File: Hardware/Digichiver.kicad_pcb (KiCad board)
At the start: 4 copper layers, 95 x 88.1 mm, 121 parts, among them J1 DM3AT-SF-PEJM5, J2 USB4105-GF-A, J3 61300211121, J4 61300211121, J5 SJ1-3535NG, SW1 PTS_647_SN50_SMTR2_LFS, SW2 PTS_647_SN50_SMTR2_LFS, SW3 PTS_647_SN50_SMTR2_LFS, U1 RP2354B, U10 TLV9004IPWR, U11 PAM8302AAD, U2 SN74LVC245A, U3 SN74LVC245A, U4 SN74LVC8T245, U5 SN74LVC8T245, U6 SN74LVC8T245, U7 TLV61046A, U8 TPSM84338, U9 PCM1809, X2 ABM8-272-T3

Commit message: generate outputs
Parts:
- C34: footprint Capacitor_SMD:C_0603_1608Metric -> Capacitor_SMD:C_0402_1005Metric
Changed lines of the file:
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@@
 		)
 	)
-	(footprint "Capacitor_SMD:C_0603_1608Metric"
+	(footprint "Capacitor_SMD:C_0402_1005Metric"
 		(layer "B.Cu")
 		(at 114.3 65.302 90)
-		(descr "Capacitor SMD 0603 (1608 Metric), square (rectangular) end terminal, IPC-7351 nominal, (Body size source: IPC-SM-782 page 76, https://www.pcb-3d.com/wordpress/wp-content/uploads/ipc-sm-782a_amendment_1_and_2.pdf)")
+		(descr "Capacitor SMD 0402 (1005 Metric), square (rectangular) end terminal, IPC-7351 nominal, (Body size source: IPC-SM-782 page 76, https://www.pcb-3d.com/wordpress/wp-content/uploads/ipc-sm-782a_amendment_1_and_2.pdf)")
 		(tags "capacitor")
 		(property "Reference" "C34"
-			(at 0 1.43 270)
-			(unlocked yes)
+			(at 0 1.16 270)
 			(layer "B.SilkS")
 			(effects
@@
 		)
 		(property "Value" "4.7uF"
-			(at 0 -1.43 90)
+			(at 0 -1.16 270)
 			(layer "B.Fab")
 			(effects
@@
 			)
 		)
-		(property "Datasheet" "https://mm.digikey.com/Volume0/opasdata/d220001/medias/docus/43/CL10A475KA8NQNC_Spec.pdf"
-			(at 0 0 90)
+		(property "Datasheet" ""
+			(at 0 0 270)
 			(layer "B.Fab")
 			(hide yes)
@@
 			)
 		)
-		(property "Description" "Unpolarized capacitor"
-			(at 0 0 90)
+		(property "Description" ""
+			(at 0 0 270)
 			(layer "B.Fab")
 			(hide yes)
@@
 		)
 		(property "KiLib_Generator" "SMD_2terminal_chip_molded"
-			(at 0 0 90)
-			(layer "B.SilkS")
-			(hide yes)
-			(effects
-				(font
-					(size 1 1)
-					(thickness 0.15)
-				)
-				(justify mirror)
-			)
-		)
-		(property "Voltage" "25V"
-			(at 0 0 270)
-			(unlocked yes)
-			(layer "B.Fab")
-			(hide yes)
-			(effects
-				(font
-					(size 1 1)
-					(thickness 0.15)
-				)
-				(justify mirror)
-			)
-		)
-		(property "MPN" "CL10A475KA8NQNC"
-			(at 0 0 270)
-			(unlocked yes)
-			(layer "B.Fab")
-			(hide yes)
-			(effects
-				(font
-					(size 1 1)
-					(thickness 0.15)
-				)
-				(justify mirror)
-			)
-		)
-		(property "KLC_S4.2_DVDD" ""
 			(at 0 0 270)
-			(unlocked yes)
-			(layer "B.Fab")
-			(hide yes)
-			(effects
-				(font
-					(size 1 1)
-					(thickness 0.15)
-				)
-				(justify mirror)
-			)
-		)
-		(property "KLC_S4.2_VREG_LX" ""
-			(at 0 0 270)
-			(unlocked yes)
-			(layer "B.Fab")
+			(layer "B.SilkS")
 			(hide yes)
 			(effects
@@
 		(duplicate_pad_numbers_are_jumpers no)
 		(fp_line
-			(start -0.14058 -0.51)
-			(end 0.14058 -0.51)
+			(start -0.107836 -0.36)
+			(end 0.107836 -0.36)
 			(stroke
 				(width 0.12)
@@
 		)
 		(fp_line
-			(start -0.14058 0.51)
-			(end 0.14058 0.51)
+			(start -0.107836 0.36)
+			(end 0.107836 0.36)
 			(stroke
 				(width 0.12)
@@
 		)
 		(fp_rect
-			(start -1.48 0.73)
-			(end 1.48 -0.73)
+			(start -0.91 0.46)
+			(end 0.91 -0.46)
 			(stroke
 				(width 0.05)
@@
 		)
 		(fp_rect
-			(start -0.8 0.4)
-			(end 0.8 -0.4)
+			(start -0.5 0.25)
+			(end 0.5 -0.25)
 			(stroke
 				(width 0.1)
@@
 		(fp_text user "${REFERENCE}"
 			(at 0 0 270)
-			(unlocked yes)
 			(layer "B.Fab")
 			(effects
 				(font
-					(size 1 1)
-					(thickness 0.15)
+					(size 0.25 0.25)
+					(thickness 0.04)
 				)
 				(justify mirror)
@@
 		)
 		(pad "1" smd roundrect
-			(at -0.775 0 90)
-			(size 0.9 0.95)
+			(at -0.48 0 90)
+			(size 0.56 0.62)
 			(layers "B.Cu" "B.Mask" "B.Paste")
 			(roundrect_rratio 0.25)
@@
 		)
 		(pad "2" smd roundrect
-			(at 0.775 0 90)
-			(size 0.9 0.95)
+			(at 0.48 0 90)
+			(size 0.56 0.62)
 			(layers "B.Cu" "B.Mask" "B.Paste")
 			(roundrect_rratio 0.25)
@@
 		)
 		(embedded_fonts no)
-		(model "${KICAD10_3DMODEL_DIR}/Capacitor_SMD.3dshapes/C_0603_1608Metric.step"
+		(model "${KICAD10_3DMODEL_DIR}/Capacitor_SMD.3dshapes/C_0402_1005Metric.step"
 			(offset
 				(xyz 0 0 0)
@@
 	)
 	(segment
+		(start 115.062 65.278)
+		(end 114.756 65.278)
+		(width 0.2)
+		(layer "B.Cu")
+		(net "GND")
+	)
+	(segment
 		(start 114.272 60.734)
 		(end 114.3 60.706)
@@
 	)
 	(segment
+		(start 114.756 65.278)
+		(end 114.3 64.822)
+		(width 0.2)
+		(layer "B.Cu")
+		(net "GND")
+	)
+	(segment
 		(start 127.96 82.24)
 		(end 128.016 82.296)
@@
 	)
 	(segment
-		(start 114.3 64.527)
-		(end 114.311 64.527)
-		(width 0.2032)
-		(layer "B.Cu")
-		(net "GND")
-	)
-	(segment
 		(start 143.215 71.669)
 		(end 142.494 72.39)
@@
 	)
 	(segment
-		(start 114.311 64.527)
-		(end 115.062 65.278)
-		(width 0.2032)
-		(layer "B.Cu")
-		(net "GND")
-	)
-	(segment
 		(start 143.908 71.669)
 		(end 143.215 71.669)
@@
 	)
 	(segment
-		(start 114.3 66.077)
-		(end 115.303 66.077)
+		(start 115.316 66.064)
+		(end 114.582 66.064)
 		(width 0.2)
 		(layer "B.Cu")
@@
 	)
 	(segment
+		(start 114.582 66.064)
+		(end 114.3 65.782)
+		(width 0.2)
+		(layer "B.Cu")
+		(net "/Power/+9V_RAW")
+	)
+	(segment
 		(start 127.757598 70.61)
 		(end 127.757598 69.854402)
@@
 	)
 	(segment
-		(start 141.235 116.6545)
-		(end 141.235 126.394471)
-		(width 0.2)
-		(layer "F.Cu")
-		(net "/Digitalker/DIGI_ROM_ADDR0")
-	)
-	(segment
 		(start 141.235 130.804)
 		(end 137.668 134.371)
@@
 	)
 	(segment
-		(start 141.235 126.394471)
-		(end 141.132 126.497471)
-		(width 0.2)
-		(layer "F.Cu")
-		(net "/Digitalker/DIGI_ROM_ADDR0")
-	)
-	(segment
-		(start 141.132 126.994529)
-		(end 141.235 127.097529)
-		(width 0.2)
-		(layer "F.Cu")
-		(net "/Digitalker/DIGI_ROM_ADDR0")
-	)
-	(segment
-		(start 141.235 127.097529)
+		(start 141.235 116.6545)
 		(end 141.235 130.804)
 		(width 0.2)
@@
 		(width 0.2)
 		(layer "F.Cu")
-		(net "/Digitalker/DIGI_ROM_ADDR0")
-	)
-	(segment
-		(start 141.132 126.497471)
-		(end 141.132 126.994529)
-		(width 0.2)
-		(layer "F.Cu")

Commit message: sync layout
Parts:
- J3, J4: footprint Connector_PinHeader_1.00mm:PinHeader_1x02_P1.00mm_Vertical -> Connector_PinHeader_2.54mm:PinHeader_1x02_P2.54mm_Vertical
- U4, U5, U6: footprint Package_SO:TSSOP-24_4.4x6.5mm_P0.5mm -> Package_SO:TSSOP-24_4.4x7.8mm_P0.65mm
- moved C6 2.92 mm to (98.2, 104.3), turned to 0 degrees
- moved C8 2.67 mm to (106.3, 128.9), turned to 0 degrees
- moved J3 1.79 mm to (147.4, 68.3)
- moved C9 1.37 mm to (106.4, 122.9)
- moved R5 1.33 mm to (106.2, 132.7)
- moved R4 1.25 mm to (98.2, 108.2)
- moved C7 1.09 mm to (98.6, 98.7)
- moved C5 0.85 mm to (104.1, 70.5)
- moved U4 0.80 mm to (106.7, 75.4)
- moved J4 0.69 mm to (118.4, 67.8)
- moved U6 0.64 mm to (109.3, 127.8)
- moved U5 0.61 mm to (101.2, 103.4)
- moved R3 0.18 mm to (101.7, 72.3)
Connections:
- R8 pad 1: /Control/D+ -> /Control/D-
- R8 pad 2: /USB_D+ -> /USB_D-
- R9 pad 1: /Control/D- -> /Control/D+
- R9 pad 2: /USB_D- -> /USB_D+
- U1 pad 66: /Control/D+ -> /Control/D-
- U1 pad 67: /Control/D- -> /Control/D+
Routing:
- net GND: track 158.0 -> 154.9 mm
- net /Digitalker/DIGI_~{CS}: track 36.9 -> 33.8 mm
- net /Digitalker/DIGI_CLK_4MHZ: track 31.6 -> 28.7 mm
- net /Digitalker/DIGI_SW6: track 33.0 -> 30.3 mm
- net /USB_D-: track 8.99 -> 7.02 mm, vias 2 -> 0
- net +9V: track 45.9 -> 44.0 mm
- net /Digitalker/DIGI_RDATA7: track 34.7 -> 33.1 mm
- net /Digitalker/DIGI_RDATA6: track 38.1 -> 36.5 mm
- net /Digitalker/DIGI_RDATA5: track 39.5 -> 38.1 mm
- net /Digitalker/DIGI_RDATA3: track 30.7 -> 29.4 mm
- net /Digitalker/DIGI_SW7: track 30.2 -> 29.0 mm
- net /Digitalker/DIGI_RDATA4: track 41.2 -> 42.4 mm
- net +3.3V: track 63.7 -> 64.6 mm
- net /USB_D+: track 8.59 -> 7.78 mm
- net /Digitalker/DIGI_CMS: track 43.5 -> 42.9 mm
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
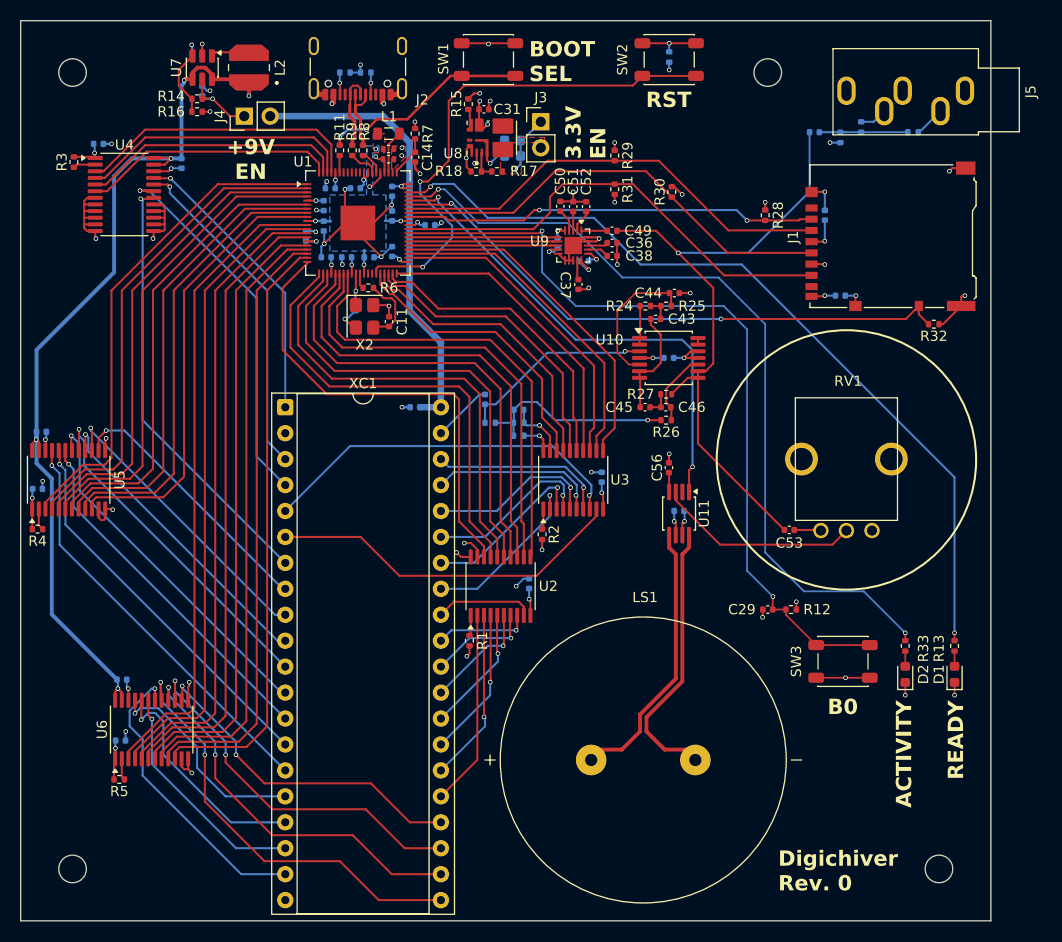
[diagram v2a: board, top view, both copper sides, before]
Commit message: update PCM1809 footprint
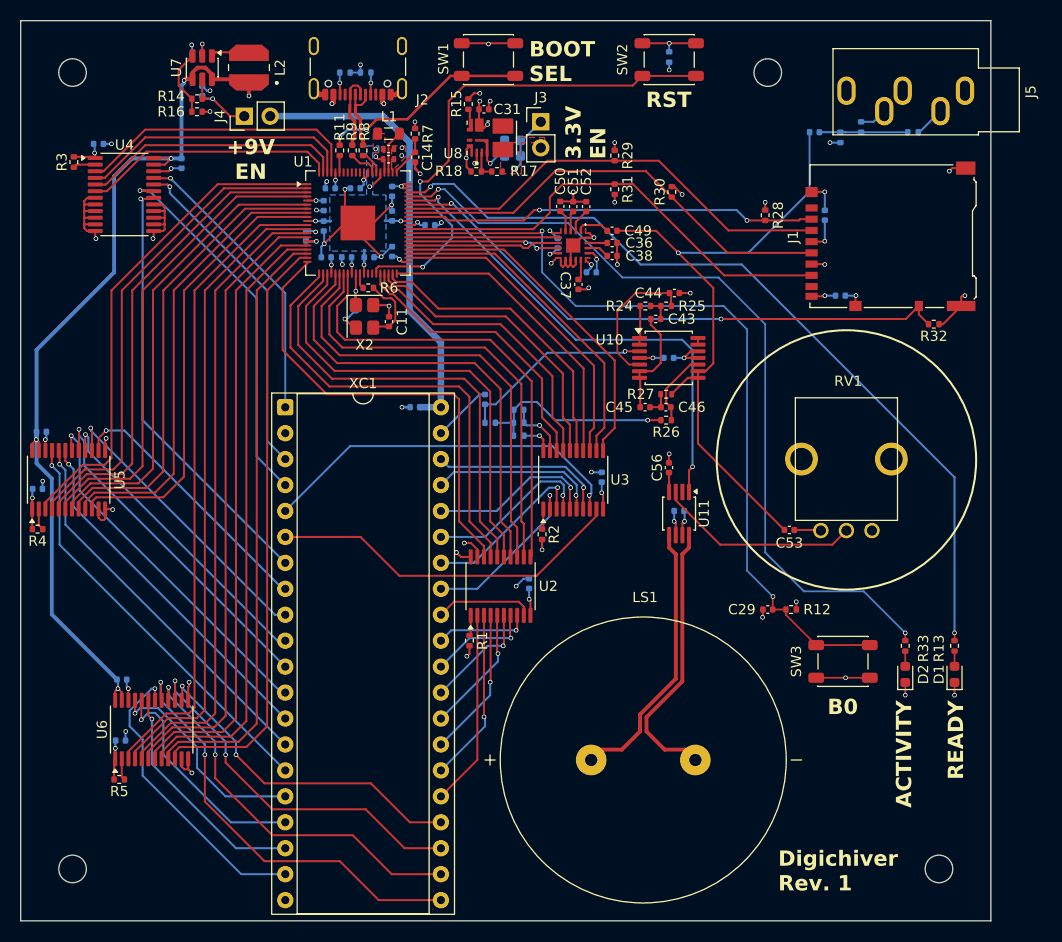
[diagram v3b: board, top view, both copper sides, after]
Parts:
- U9: footprint Package_DFN_QFN:WQFN-20-1EP_3x3mm_P0.4mm_EP1.7x1.7mm -> Digichiver:PCM1820IRTER
- moved C40 1.34 mm to (152.4, 83.1)
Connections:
- U1 pad 45: /FSYNC -> /BCLK
- U1 pad 46: /BCLK -> /FSYNC
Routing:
- net GND: track 154.9 -> 155.8 mm, vias 60 -> 61
- net /Audio/RECORDED_SPEECH: track 2.54 -> 3.27 mm
- net +3.3V: track 64.6 -> 65.2 mm
- net /FSYNC: track 14.7 -> 15.0 mm, vias 0 -> 2
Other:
- board text added: "Digichiver Rev. 1"
- board text removed: "Digichiver Rev. 0"

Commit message: reset 3V3 -> 5V shifter passives to match original stencil
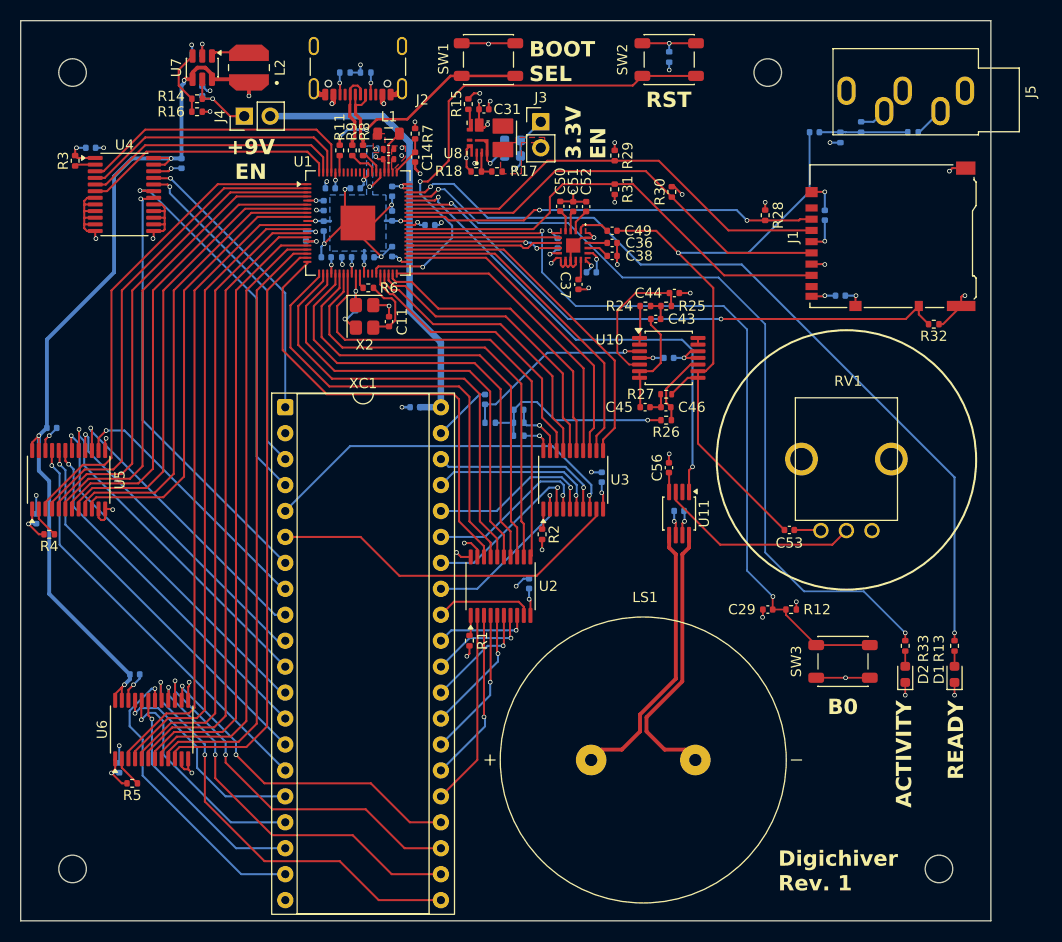
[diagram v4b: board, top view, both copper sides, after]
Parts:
- moved C6 2.92 mm to (98.0, 107.2), turned to 90 degrees
- moved C8 2.67 mm to (106.2, 131.6), turned to 90 degrees
- moved C9 1.37 mm to (107.7, 122.4)
- moved R5 1.33 mm to (107.4, 133.1)
- moved R4 1.25 mm to (99.3, 108.7)
- moved C7 1.09 mm to (99.6, 98.3)
- moved C5 0.85 mm to (103.4, 70.9)
- moved R3 0.18 mm to (101.9, 72.1)
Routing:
- net GND: track 155.8 -> 159.1 mm
- net +5V: track 97.8 -> 99.3 mm
- net +3.3V: track 65.2 -> 66.3 mm
- net Net-(U5-DIR): track 2.13 -> 3.11 mm
- net Net-(U6-DIR): track 2.13 -> 3.04 mm

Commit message: update orange LED net name
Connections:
- net /Control/LED_RED renamed /Control/LED_OR
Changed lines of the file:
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@@
 			)
 		)
-		(property "Color" "AMBER"
+		(property "Color" "ORANGE"
 			(at 0 0 90)
 			(unlocked yes)
@@
 			(layers "F.Cu" "F.Mask" "F.Paste")
 			(roundrect_rratio 0.25)
-			(net "/Control/LED_RED")
+			(net "/Control/LED_OR")
 			(pintype "passive")
 		)
@@
 			(layers "F.Cu" "F.Mask" "F.Paste")
 			(roundrect_rratio 0.25)
-			(net "/Control/LED_RED")
+			(net "/Control/LED_OR")
 			(pinfunction "GPIO46/ADC6_57")
 			(pintype "bidirectional")
@@
 	)
 	(segment
-		(start 136.712 75.632)
-		(end 134.49 75.632)
-		(width 0.2)
-		(layer "F.Cu")
-		(net "/Control/LED_RED")
-	)
-	(segment
-		(start 183.134 119.124)
-		(end 183.134 118.364)
-		(width 0.1778)
-		(layer "F.Cu")
-		(net "/Control/LED_RED")
-	)
-	(segment
-		(start 137.414 74.93)
-		(end 136.712 75.632)
-		(width 0.2)
-		(layer "F.Cu")
-		(net "/Control/LED_RED")
-	)
-	(via
-		(at 137.414 74.93)
-		(size 0.45)
-		(drill 0.3)
-		(layers "F.Cu" "B.Cu")
-		(net "/Control/LED_RED")
-	)
-	(via
-		(at 183.134 118.364)
-		(size 0.45)
-		(drill 0.3)
-		(layers "F.Cu" "B.Cu")
-		(net "/Control/LED_RED")
-	)
-	(segment
-		(start 169.418 110.49)
-		(end 169.418 88.138)
-		(width 0.1778)
-		(layer "B.Cu")
-		(net "/Control/LED_RED")
-	)
-	(segment
-		(start 173.228 114.3)
-		(end 169.418 110.49)
-		(width 0.1778)
-		(layer "B.Cu")
-		(net "/Control/LED_RED")
-	)
-	(segment
-		(start 138.033765 74.93)
-		(end 137.414 74.93)
-		(width 0.1778)
-		(layer "B.Cu")
-		(net "/Control/LED_RED")
-	)
-	(segment
-		(start 183.134 118.364)
-		(end 179.07 114.3)
-		(width 0.1778)
-		(layer "B.Cu")
-		(net "/Control/LED_RED")
-	)
-	(segment
-		(start 150.114 78.232)
-		(end 141.335765 78.232)
-		(width 0.1778)
-		(layer "B.Cu")
-		(net "/Control/LED_RED")
-	)
-	(segment
-		(start 169.418 88.138)
-		(end 164.846 83.566)
-		(width 0.1778)
-		(layer "B.Cu")
-		(net "/Control/LED_RED")
-	)
-	(segment
-		(start 179.07 114.3)
-		(end 173.228 114.3)
-		(width 0.1778)
-		(layer "B.Cu")
-		(net "/Control/LED_RED")
-	)
-	(segment
-		(start 164.846 83.566)
-		(end 155.448 83.566)
-		(width 0.1778)
-		(layer "B.Cu")
-		(net "/Control/LED_RED")
-	)
-	(segment
-		(start 155.448 83.566)
-		(end 150.114 78.232)
-		(width 0.1778)
-		(layer "B.Cu")
-		(net "/Control/LED_RED")
-	)
-	(segment
-		(start 141.335765 78.232)
-		(end 138.033765 74.93)
-		(width 0.1778)
-		(layer "B.Cu")
-		(net "/Control/LED_RED")
-	)
-	(segment
 		(start 130.79 65.656)
 		(end 130.79 64.536)
@@
 		(net "Net-(C55-Pad1)")
 	)
+	(segment
+		(start 136.712 75.632)
+		(end 134.49 75.632)
+		(width 0.2)
+		(layer "F.Cu")
+		(net "/Control/LED_OR")
+	)
+	(segment
+		(start 183.134 119.124)
+		(end 183.134 118.364)
+		(width 0.1778)
+		(layer "F.Cu")
+		(net "/Control/LED_OR")
+	)
+	(segment
+		(start 137.414 74.93)
+		(end 136.712 75.632)
+		(width 0.2)
+		(layer "F.Cu")
+		(net "/Control/LED_OR")
+	)
+	(via
+		(at 137.414 74.93)
+		(size 0.45)
+		(drill 0.3)
+		(layers "F.Cu" "B.Cu")
+		(net "/Control/LED_OR")
+	)
+	(via
+		(at 183.134 118.364)
+		(size 0.45)
+		(drill 0.3)
+		(layers "F.Cu" "B.Cu")
+		(net "/Control/LED_OR")
+	)
+	(segment
+		(start 169.418 110.49)
+		(end 169.418 88.138)
+		(width 0.1778)
+		(layer "B.Cu")
+		(net "/Control/LED_OR")
+	)
+	(segment
+		(start 173.228 114.3)
+		(end 169.418 110.49)
+		(width 0.1778)
+		(layer "B.Cu")
+		(net "/Control/LED_OR")
+	)
+	(segment
+		(start 138.033765 74.93)
+		(end 137.414 74.93)
+		(width 0.1778)
+		(layer "B.Cu")
+		(net "/Control/LED_OR")
+	)
+	(segment
+		(start 183.134 118.364)
+		(end 179.07 114.3)
+		(width 0.1778)
+		(layer "B.Cu")
+		(net "/Control/LED_OR")
+	)
+	(segment
+		(start 150.114 78.232)
+		(end 141.335765 78.232)
+		(width 0.1778)
+		(layer "B.Cu")
+		(net "/Control/LED_OR")
+	)
+	(segment
+		(start 169.418 88.138)
+		(end 164.846 83.566)
+		(width 0.1778)
+		(layer "B.Cu")
+		(net "/Control/LED_OR")
+	)
+	(segment
+		(start 179.07 114.3)
+		(end 173.228 114.3)
+		(width 0.1778)
+		(layer "B.Cu")
+		(net "/Control/LED_OR")
+	)
+	(segment
+		(start 164.846 83.566)
+		(end 155.448 83.566)
+		(width 0.1778)
+		(layer "B.Cu")
+		(net "/Control/LED_OR")
+	)
+	(segment
+		(start 155.448 83.566)
+		(end 150.114 78.232)
+		(width 0.1778)
+		(layer "B.Cu")
+		(net "/Control/LED_OR")
+	)
+	(segment
+		(start 141.335765 78.232)
+		(end 138.033765 74.93)
+		(width 0.1778)
+		(layer "B.Cu")
+		(net "/Control/LED_OR")
+	)
 	(zone
